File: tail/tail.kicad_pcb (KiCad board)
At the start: 2 copper layers, 119.8 x 200 mm, 3 parts

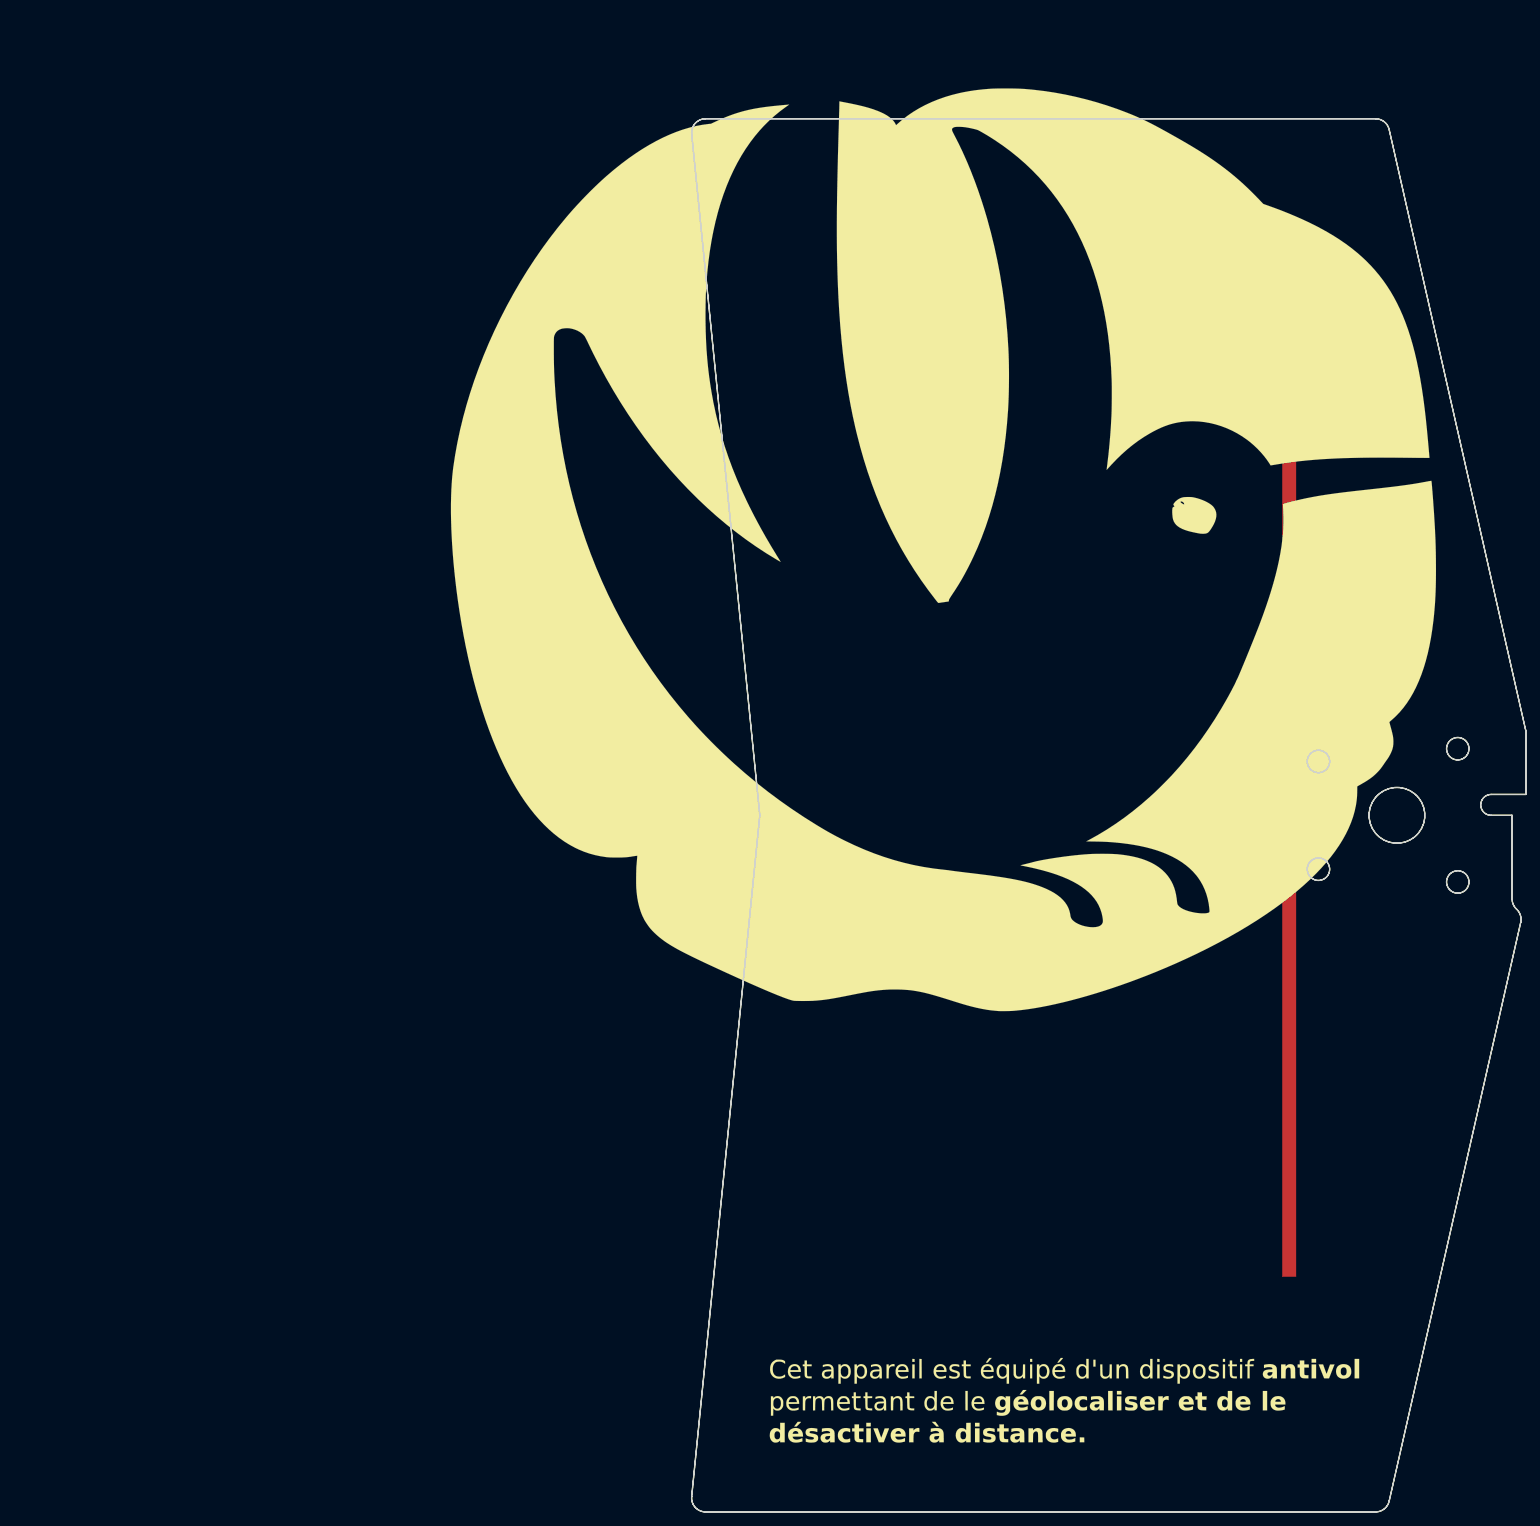
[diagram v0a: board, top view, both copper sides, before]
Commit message: remove pioupiou logo
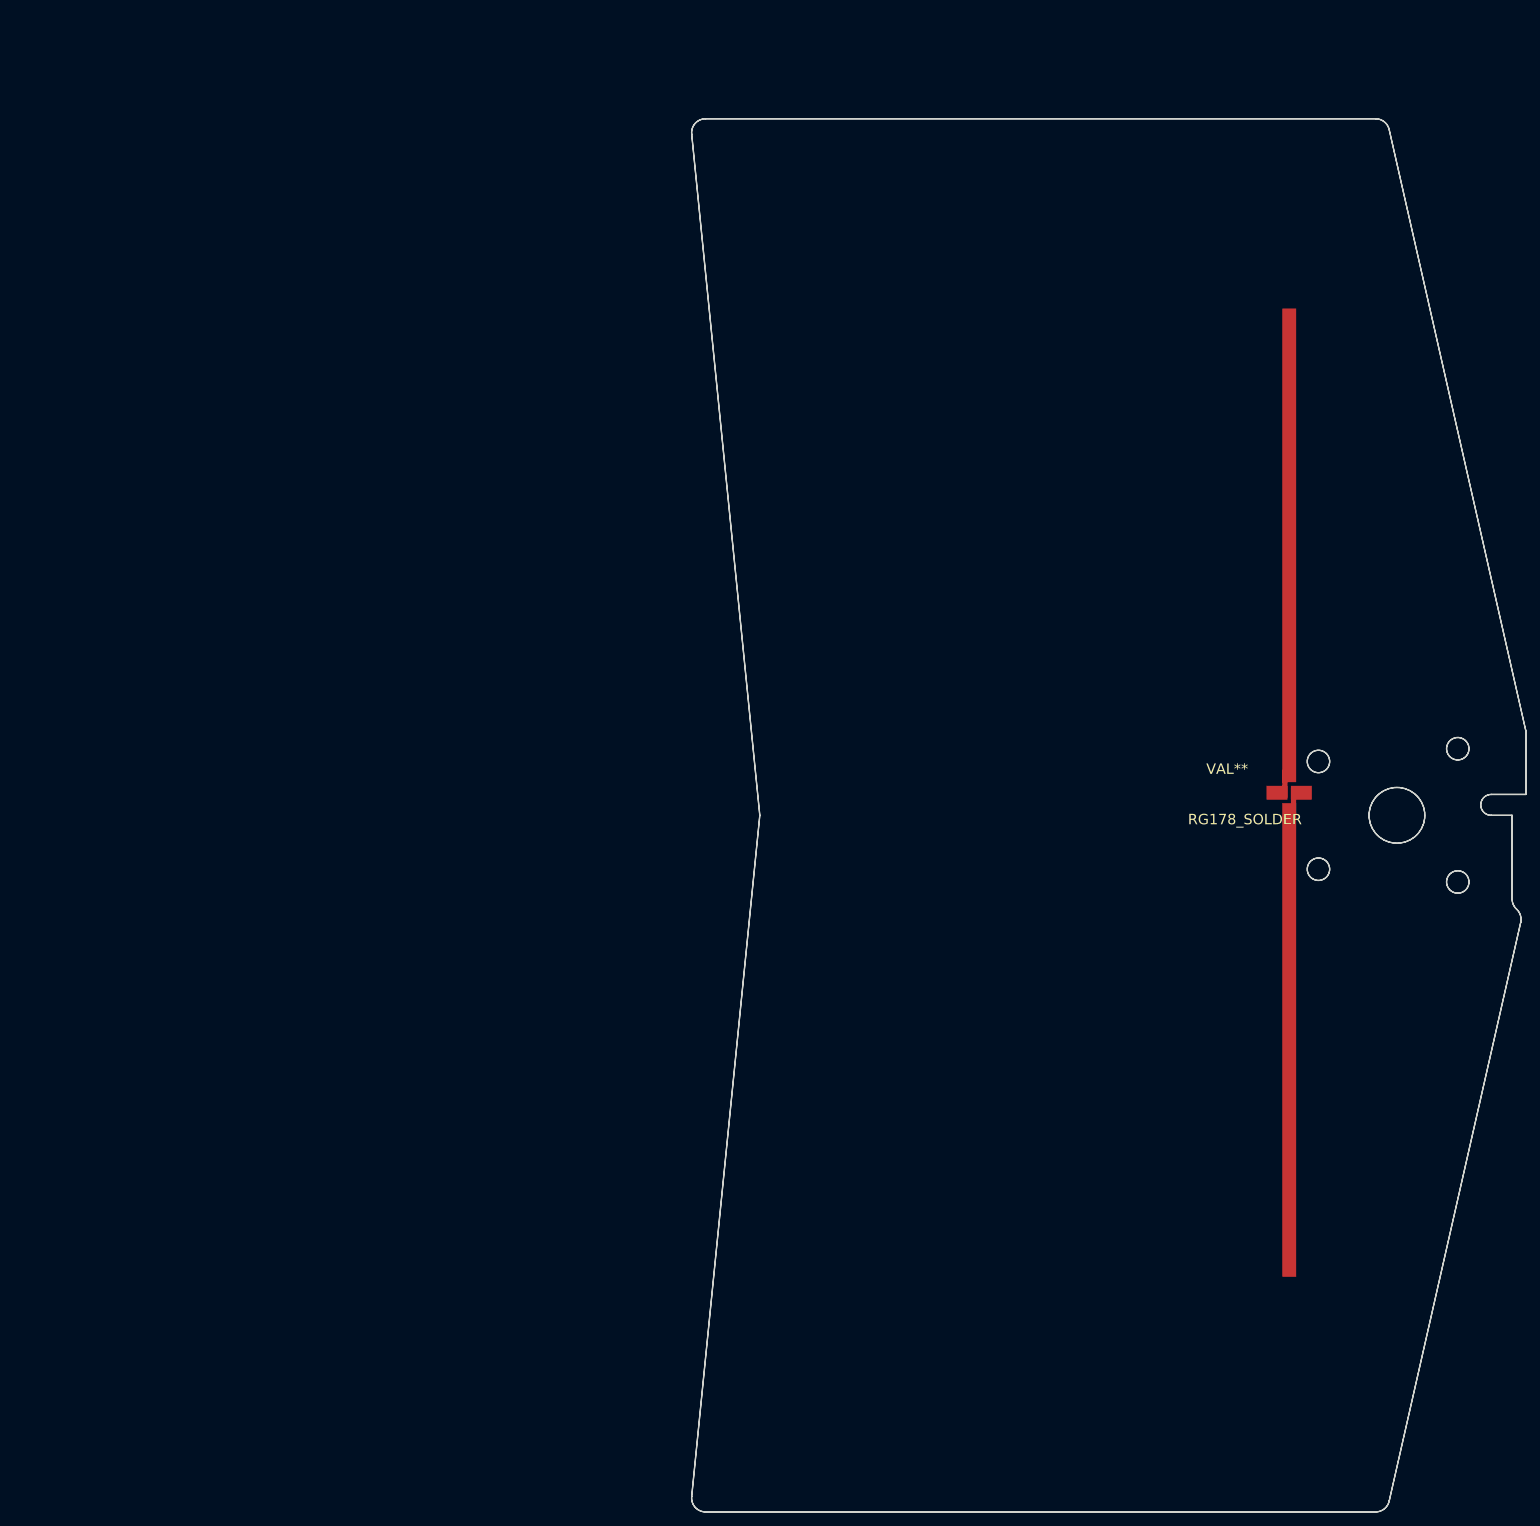
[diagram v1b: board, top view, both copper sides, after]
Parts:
- removed G***: LOGO, libraries:tail-artwork-B-new
- removed VAL: REF, tail-artwork-a-ready:tail-artwork-a-ready

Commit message: tune antenna for weigth and resonance frequency
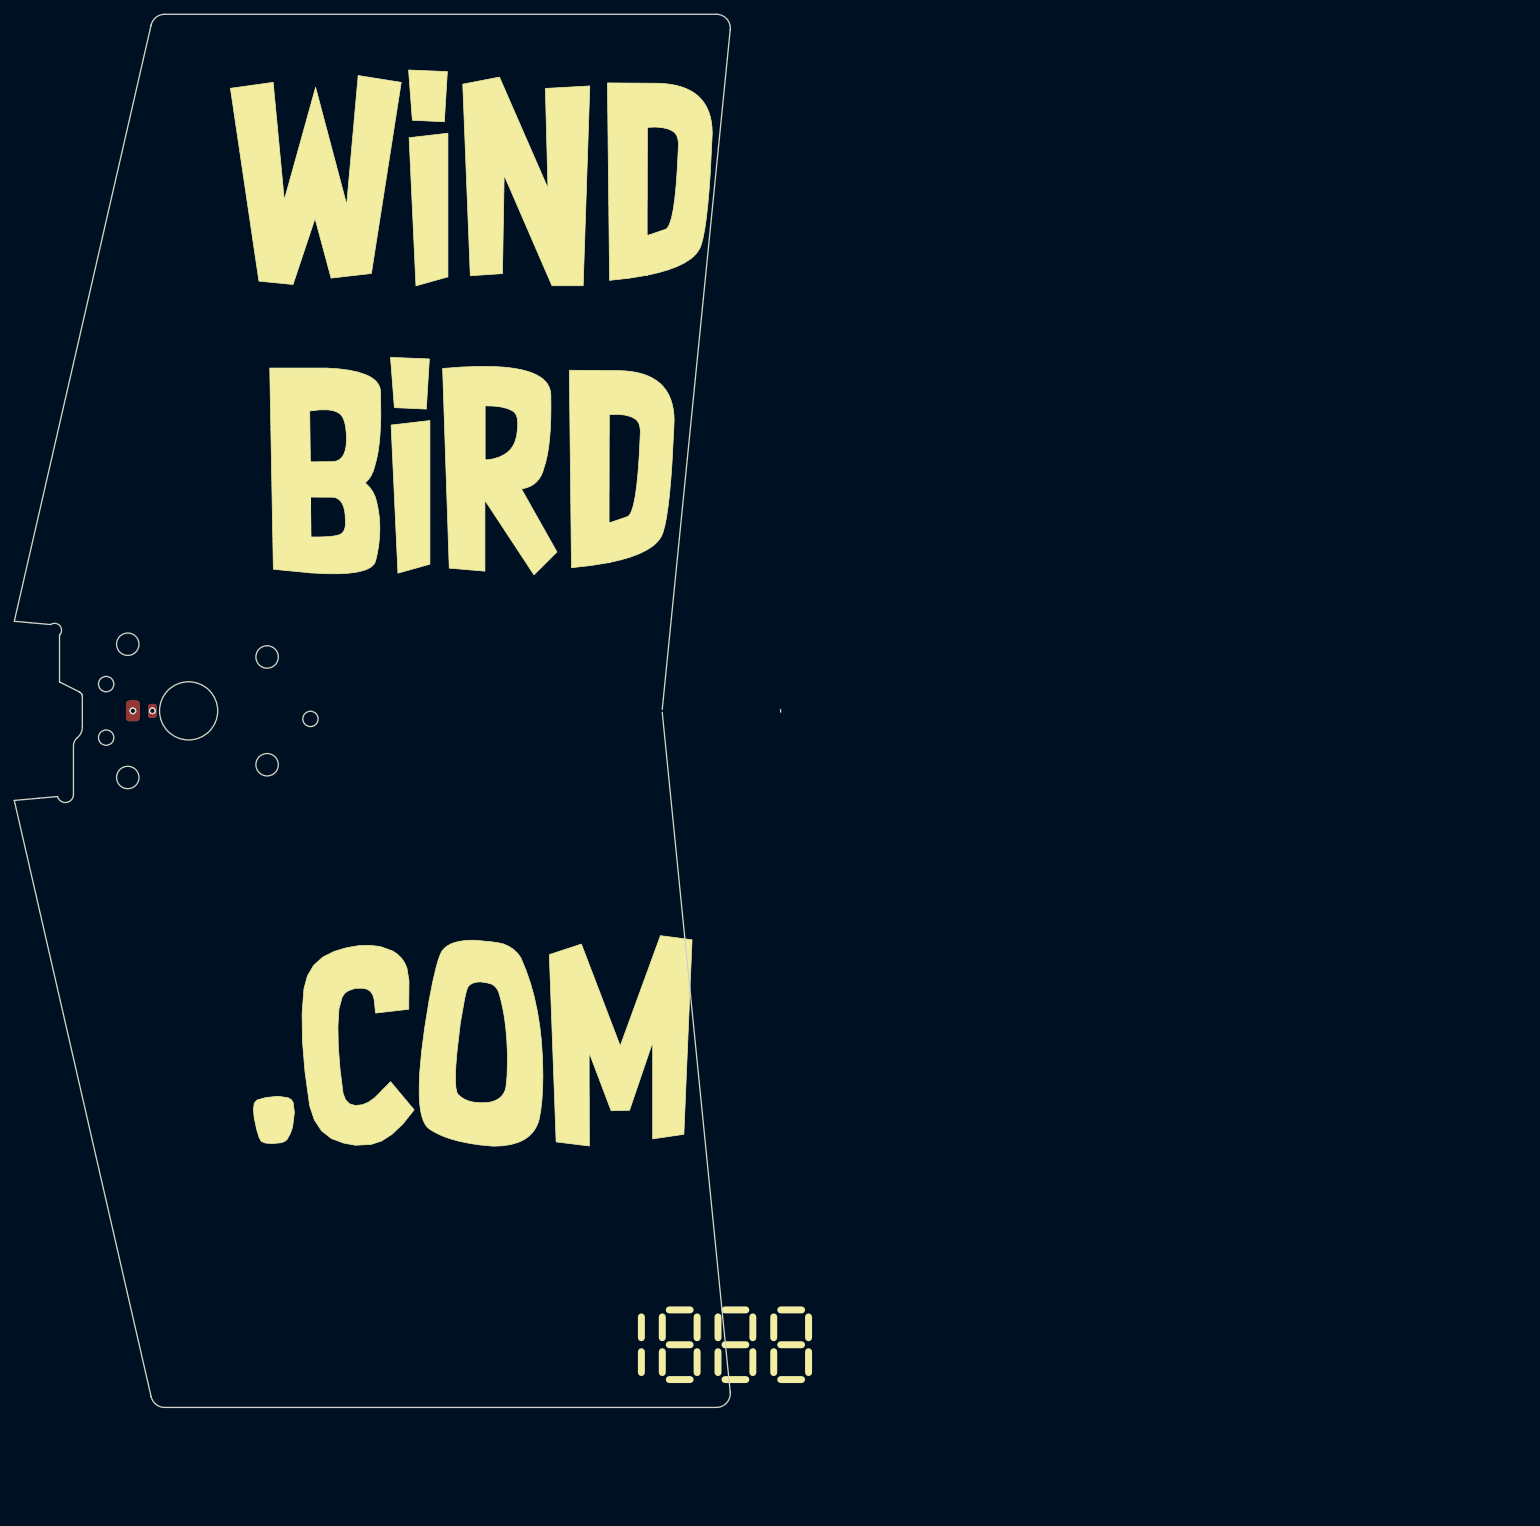
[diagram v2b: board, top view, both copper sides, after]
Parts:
- removed RG178_SOLDER: VAL**, RG178_SOLDER
- added REF**: tail_branding, windbird:tail_branding, F.Cu at (74.0, 43.0)
- added REF**: tail_antenna_cable, windbird:tail_antenna_cable, F.Cu at (62.8, 135.0)
- added REF**: tail_branding, windbird:tail_branding, B.Cu at (144.0, 42.5)
- added REF**: CE-Logo_8.5x6mm_SilkScreen, Symbol:CE-Logo_8.5x6mm_SilkScreen, B.Cu at (69.0, 228.0)
- added REF**: WEEE-Logo_4.2x6mm_SilkScreen, Symbol:WEEE-Logo_4.2x6mm_SilkScreen, B.Cu at (78.0, 228.0)
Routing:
- net (no net): track 0.00 -> 21.2 mm, vias 0 -> 2
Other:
- board size 119.8 x 200 mm -> 110 x 200 mm
- copper layers 2 -> 4
- net class Default removed

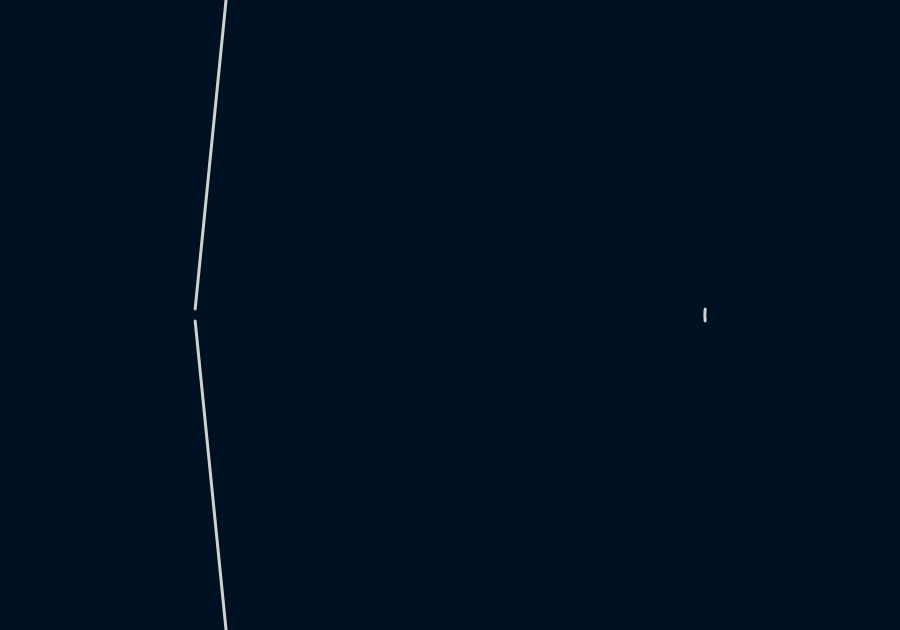
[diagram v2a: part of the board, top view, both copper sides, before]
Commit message: fix broken contour
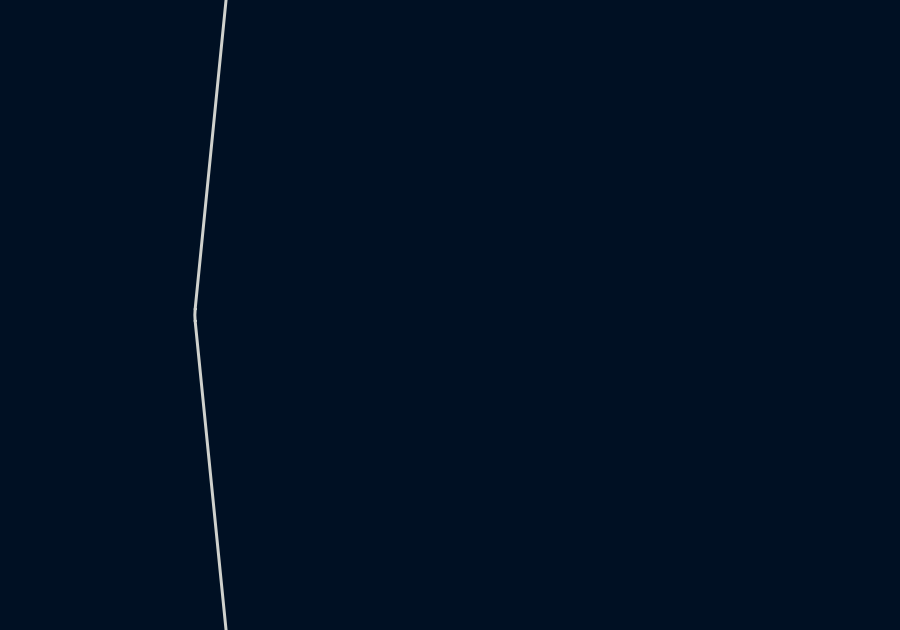
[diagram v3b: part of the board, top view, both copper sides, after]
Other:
- board size 110 x 200 mm -> 102.8 x 200 mm
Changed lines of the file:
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@@
   (gr_line (start 135.993018 135.199007) (end 145.753217 232.800992)
     (stroke (width 0.1) (type solid)) (layer "Edge.Cuts"))
-  (gr_arc (start 152.993018 135.199008) (mid 152.983092 135) (end 152.993018 134.800993)
+  (gr_arc (start 135.993018 135.199008) (mid 135.983092 135.000001) (end 135.993018 134.800993)
     (stroke (width 0.1) (type solid)) (layer "Edge.Cuts"))
   (gr_arc (start 51.467094 147) (mid 50.458882 148.148783) (end 49.188961 147.298198)
